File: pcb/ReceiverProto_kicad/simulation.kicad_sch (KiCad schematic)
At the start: 2 parts

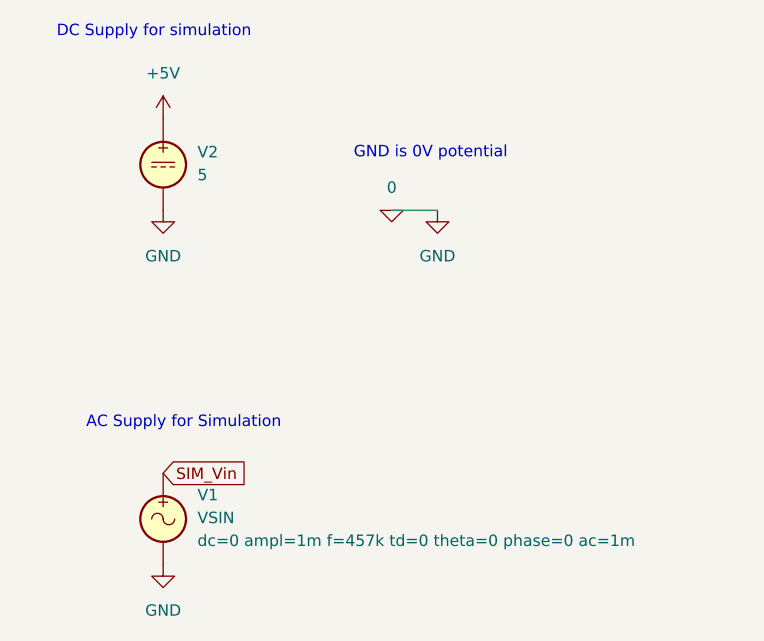
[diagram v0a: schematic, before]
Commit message: added libries and footprints for op amp.
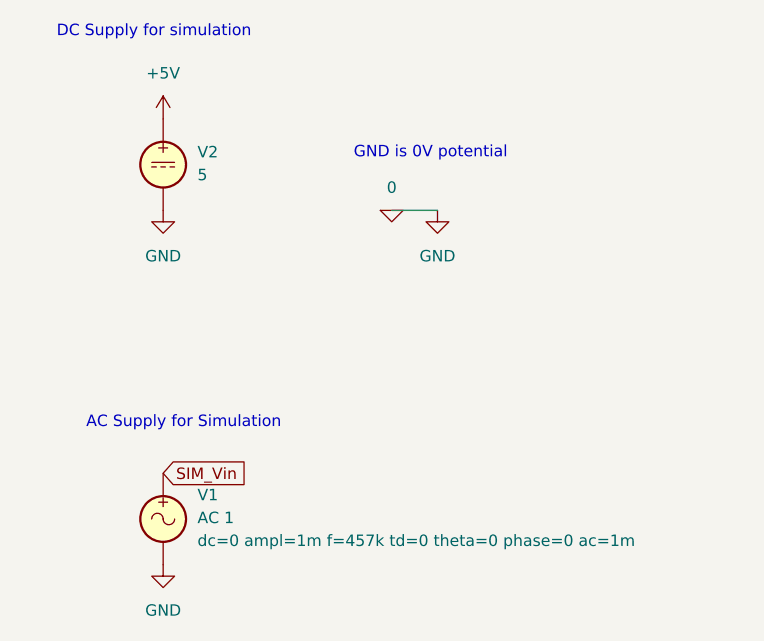
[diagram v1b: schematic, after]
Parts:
- V1: value VSIN -> AC 1
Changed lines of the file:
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@@
 			)
 		)
-		(property "Value" "VSIN"
+		(property "Value" "AC 1"
 			(at 143.51 125.6001 0)
 			(effects

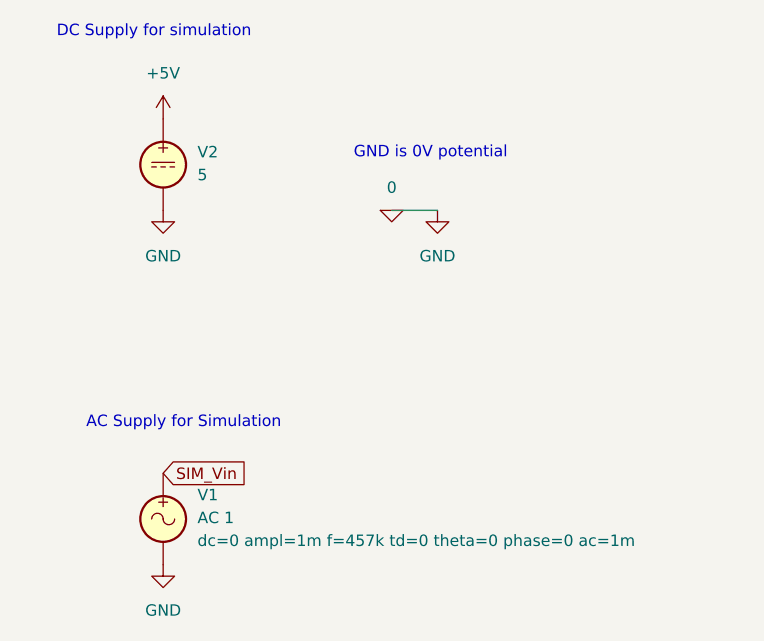
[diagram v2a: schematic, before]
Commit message: 0 net is now gnd; changed power routing to inner copper layer 2; added labels; few tweaks to routing and track width; arranged component identifiers
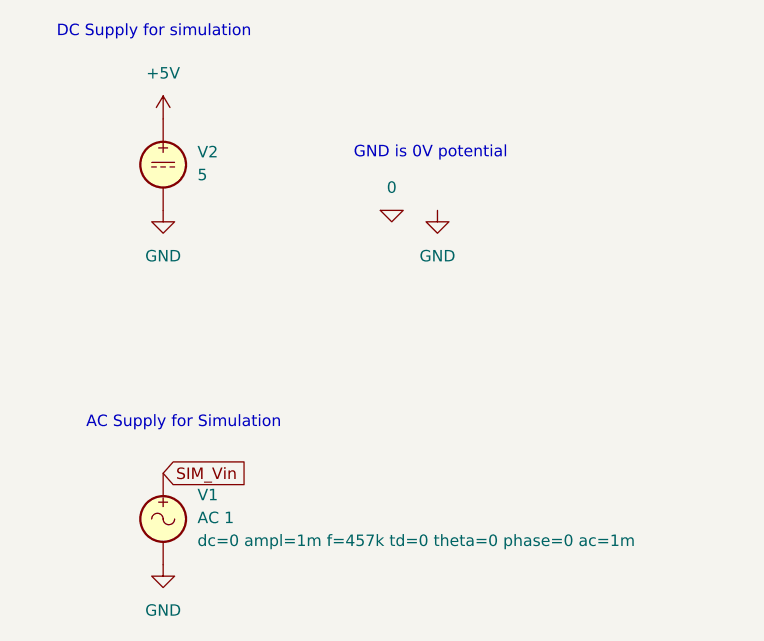
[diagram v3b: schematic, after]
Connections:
- net 0: no longer V1.2, V2.2
- new net GND: V1.2, V2.2
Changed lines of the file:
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@@
-		)
-	)
-	(wire
-		(pts
-			(xy 165.1 91.44) (xy 170.18 91.44)
-		)
-		(stroke
-			(width 0)
-			(type default)
 		)
 	)
